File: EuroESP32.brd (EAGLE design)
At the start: 30 x 108 mm, 117 parts, among them IC1 TL074D, IC10 MCP6004, IC2 TL072, IC3 TL072, IC4 WM8731, IC5 TL074D, IC7 ADP7118, P4 POWER_SIMPLE10, U1 LM4040SOT23, U2 MCP3204-CI/SL

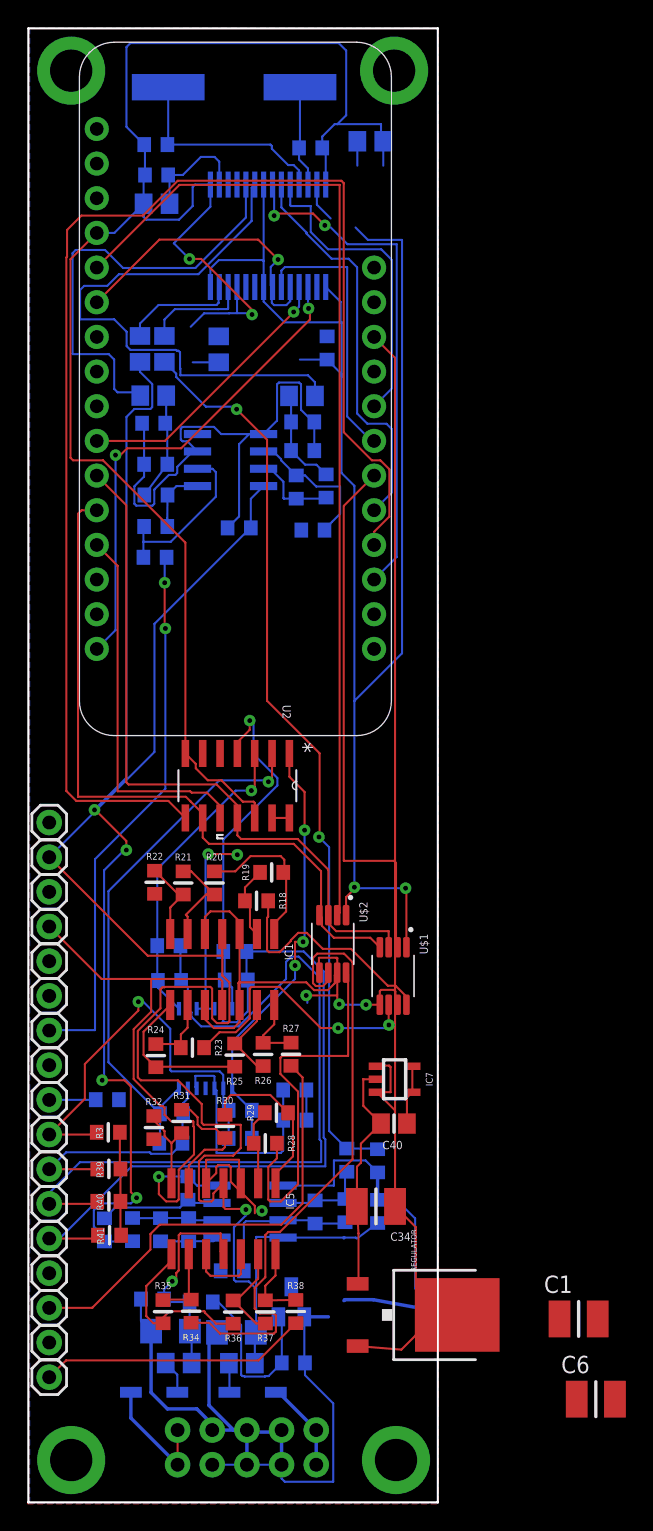
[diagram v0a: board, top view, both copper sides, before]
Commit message: Update EuroESP32.brd
v0.2
Proper spacing for the main connector
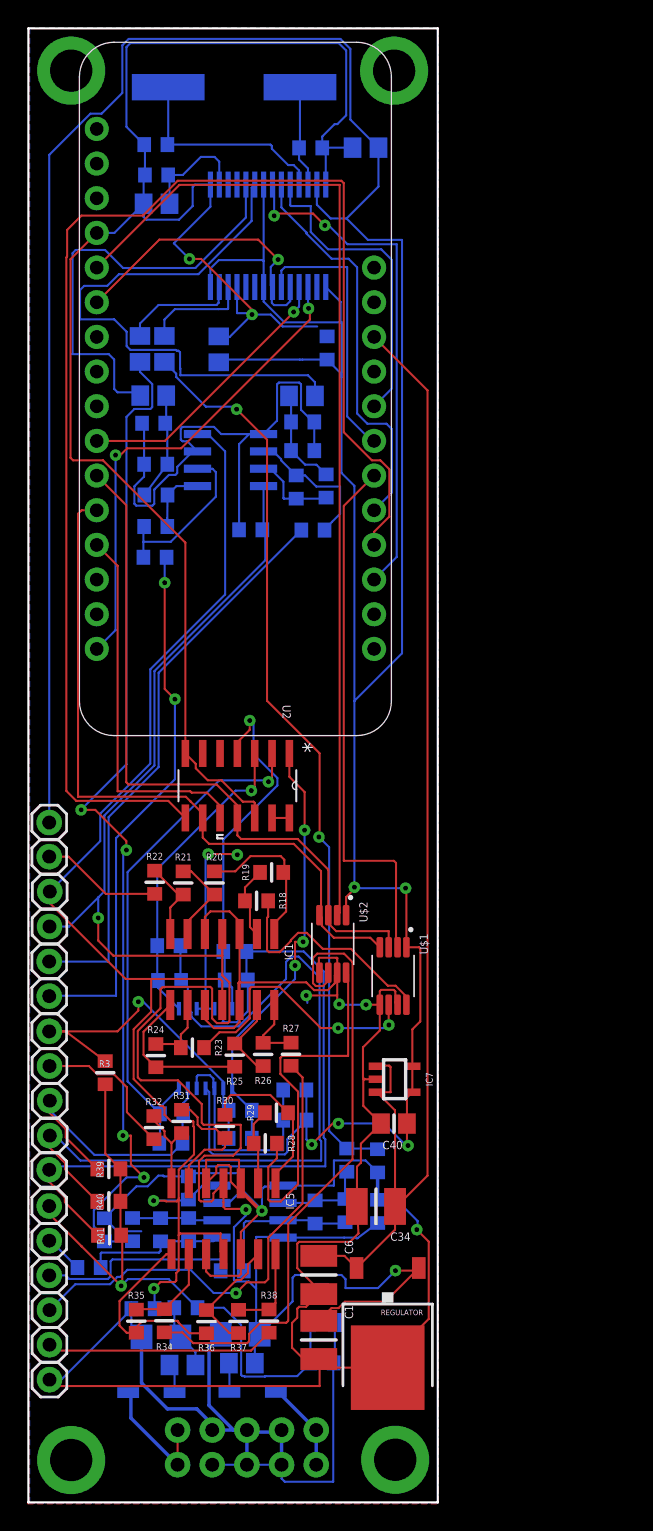
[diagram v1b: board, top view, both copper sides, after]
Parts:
- moved GND 35.7 mm to (1.55, 8.99)
- moved CVOUT1 30.5 mm to (1.53, 47.3)
- moved C6 22.2 mm to (21.3, 16.7), turned to 270 degrees
- moved CVOUT3 20.3 mm to (1.55, 32.0)
- moved C1 19.1 mm to (21.3, 11.9), turned to 270 degrees
- moved -10VREF 17.9 mm to (1.53, 21.7)
- moved J_LOUT 15.4 mm to (1.53, 16.6)
- moved R12 12.4 mm to (4.45, 17.2)
- moved J_ROUT 10.3 mm to (1.53, 19.2)
- moved CVIN(100K)0 7.56 mm to (1.53, 34.5)
- moved +12V 5.08 mm to (1.55, 42.2)
- moved CVIN(100K)3 5.04 mm to (1.53, 24.4)
- moved CVIN(100K)1 5.02 mm to (1.57, 29.4)
- moved CVIN(100K)2 5.00 mm to (1.57, 26.9)
- moved R3 4.37 mm to (5.63, 31.5), turned to 270 degrees
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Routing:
- net +3.3VA: track 131.6 -> 262.7 mm, vias 2 -> 5
- net GND: track 378.9 -> 446.2 mm, vias 8 -> 9
- net -12V: track 60.2 -> 105.3 mm
- net N$1: track 0.00 -> 41.8 mm
- net +12V: track 122.2 -> 150.0 mm, vias 1 -> 3
- net -10VREF: track 20.9 -> 45.9 mm, vias 0 -> 1
- net N$2: track 0.00 -> 14.7 mm
- net N$29: track 0.00 -> 10.9 mm
- net N$25: track 0.00 -> 8.86 mm
- net N$46: track 4.25 -> 10.5 mm
- net N$17: track 31.0 -> 25.6 mm
- net N$19: track 18.4 -> 22.8 mm
- net N$34: track 19.7 -> 16.8 mm
- net N$27: track 32.8 -> 35.4 mm, vias 0 -> 1
- net N$23: track 13.0 -> 14.7 mm
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
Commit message: Added extra connectors
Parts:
- added P1: A2/I34, TOF:1X01_SIDE_NAME
- added P2: A3/I39, TOF:1X01_SIDE_NAME
- added P3: A4/I36, TOF:1X01_SIDE_NAME
- added P5: RX/IO16, TOF:1X01_SIDE_NAME
- added P6: TX/IO17, TOF:1X01_SIDE_NAME
- added P7: SDA, TOF:1X01_SIDE_NAME
- added P8: SCL, TOF:1X01_SIDE_NAME
- added P9: IO13, TOF:1X01_SIDE_NAME
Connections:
- new net N$30: MS2.8, P2.1
- new net N$35: MS2.9, P3.1
- new net N$38: MS2.14, P5.1
- new net N$39: MS2.15, P6.1
- new net N$41: MS2.17, P7.1
- new net N$50: MS2.18, P8.1
- new net N$51: MS2.25, P9.1
- new net N$7: MS2.7, P1.1
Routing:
- net N$41: track 0.00 -> 74.2 mm
- net N$50: track 0.00 -> 62.9 mm, vias 0 -> 2
- net N$51: track 0.00 -> 59.6 mm, vias 0 -> 1
- net +3.3VA: track 262.7 -> 208.7 mm, vias 5 -> 6
- net ADC_CS: track 101.2 -> 66.4 mm, vias 0 -> 2
- net N$38: track 0.00 -> 11.7 mm
- net N$39: track 0.00 -> 11.7 mm
- net N$7: track 0.00 -> 8.32 mm, vias 0 -> 1
- net N$30: track 0.00 -> 5.62 mm
- net N$35: track 0.00 -> 3.51 mm
- net LIN: track 41.3 -> 42.4 mm

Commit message: Added a little information
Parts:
- D1, D2: value (none) -> 1N5819HW
- F1, F2: value FERRITE-BEAD0805 -> Würth Electronics 742792664
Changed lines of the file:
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@@
 </element>
 <element name="P4" library="parts_aman" package="POWER_10" value="POWER_SIMPLE10" x="16.015" y="4.028" smashed="yes" rot="MR180" grouprefs="POWER_IN"/>
-<element name="D1" library="parts_aman" package="SOD123" value="" x="16.435" y="8.065" smashed="yes" rot="MR180" grouprefs="POWER_IN">
+<element name="D1" library="parts_aman" package="SOD123" value="1N5819HW" x="16.435" y="8.065" smashed="yes" rot="MR180" grouprefs="POWER_IN">
 <attribute name="NAME" x="13.26" y="8.065" size="0.508" layer="26" font="vector" ratio="16" rot="MR270" align="center"/>
 </element>
-<element name="D2" library="parts_aman" package="SOD123" value="" x="9.015" y="8.045" smashed="yes" rot="MR180" grouprefs="POWER_IN">
+<element name="D2" library="parts_aman" package="SOD123" value="1N5819HW" x="9.015" y="8.045" smashed="yes" rot="MR180" grouprefs="POWER_IN">
 <attribute name="NAME" x="5.84" y="8.045" size="0.508" layer="26" font="vector" ratio="16" rot="MR270" align="center"/>
 </element>
-<element name="F1" library="parts_aman" package="R0805" value="FERRITE-BEAD0805" x="15.645" y="10.195" smashed="yes" rot="MR0" grouprefs="POWER_IN">
+<element name="F1" library="parts_aman" package="R0805" value="Würth Electronics 742792664" x="15.645" y="10.195" smashed="yes" rot="MR0" grouprefs="POWER_IN">
 <attribute name="NAME" x="17.55" y="10.195" size="0.508" layer="26" font="vector" ratio="16" rot="MR90" align="center"/>
 </element>
-<element name="F2" library="parts_aman" package="R0805" value="FERRITE-BEAD0805" x="11.295" y="10.065" smashed="yes" rot="MR0" grouprefs="POWER_IN">
+<element name="F2" library="parts_aman" package="R0805" value="Würth Electronics 742792664" x="11.295" y="10.065" smashed="yes" rot="MR0" grouprefs="POWER_IN">
 <attribute name="NAME" x="9.39" y="10.065" size="0.508" layer="26" font="vector" ratio="16" rot="MR90" align="center"/>
 </element>
